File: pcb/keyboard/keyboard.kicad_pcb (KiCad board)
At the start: 2 copper layers, 137.2 x 109.2 mm, 96 parts, among them J1 Audio-Jack-4, J2 sidebutton, SW1 RESET_SW, U1 Arduino_Pro_Micro, U2 Arduino_Pro_Micro

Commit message: add LED
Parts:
- added D53: LED, LEDs:LED_D3.0mm, F.Cu at (116.2, 39.4)
- added D54: LED, LEDs:LED_D3.0mm, F.Cu at (116.2, 43.8)
- added D55: LED, LEDs:LED_D3.0mm, F.Cu at (116.2, 48.3)
- added R3: 100Ω, Resistors_THT:R_Axial_DIN0204_L3.6mm_D1.6mm_P7.62mm_Horizontal, F.Cu at (119.4, 28.6)
- added R5: 100Ω, Resistors_THT:R_Axial_DIN0204_L3.6mm_D1.6mm_P7.62mm_Horizontal, F.Cu at (117.5, 28.6)
- added R6: 100Ω, Resistors_THT:R_Axial_DIN0204_L3.6mm_D1.6mm_P7.62mm_Horizontal, F.Cu at (115.6, 28.6)
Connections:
- U1 pad 18: Net-(U1-Pad18) -> /LED3
- U1 pad 19: Net-(U1-Pad19) -> /LED2
- U1 pad 20: Net-(U1-Pad20) -> /LED1
- U2 pad 18: Net-(U2-Pad18) -> /LED3
- U2 pad 19: Net-(U2-Pad19) -> /LED2
- U2 pad 20: Net-(U2-Pad20) -> /LED1
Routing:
- net /LED3: track 0.00 -> 56.0 mm, vias 0 -> 11
- net /LED2: track 0.00 -> 54.1 mm, vias 0 -> 14
- net /LED1: track 0.00 -> 52.8 mm, vias 0 -> 16
- net +5V: track 82.9 -> 101.7 mm, vias 1 -> 2
- net Net-(D55-Pad2): track 0.00 -> 14.1 mm
- net Net-(D54-Pad2): track 0.00 -> 8.15 mm
- net Net-(D53-Pad2): track 0.00 -> 3.44 mm
- net /SDA: track 65.7 -> 68.0 mm
- net /ROW4: track 300.2 -> 301.8 mm
- net /COL0: track 110.5 -> 112.1 mm
- net /SCL: track 60.0 -> 61.4 mm
- net /COL4: track 153.4 -> 153.9 mm

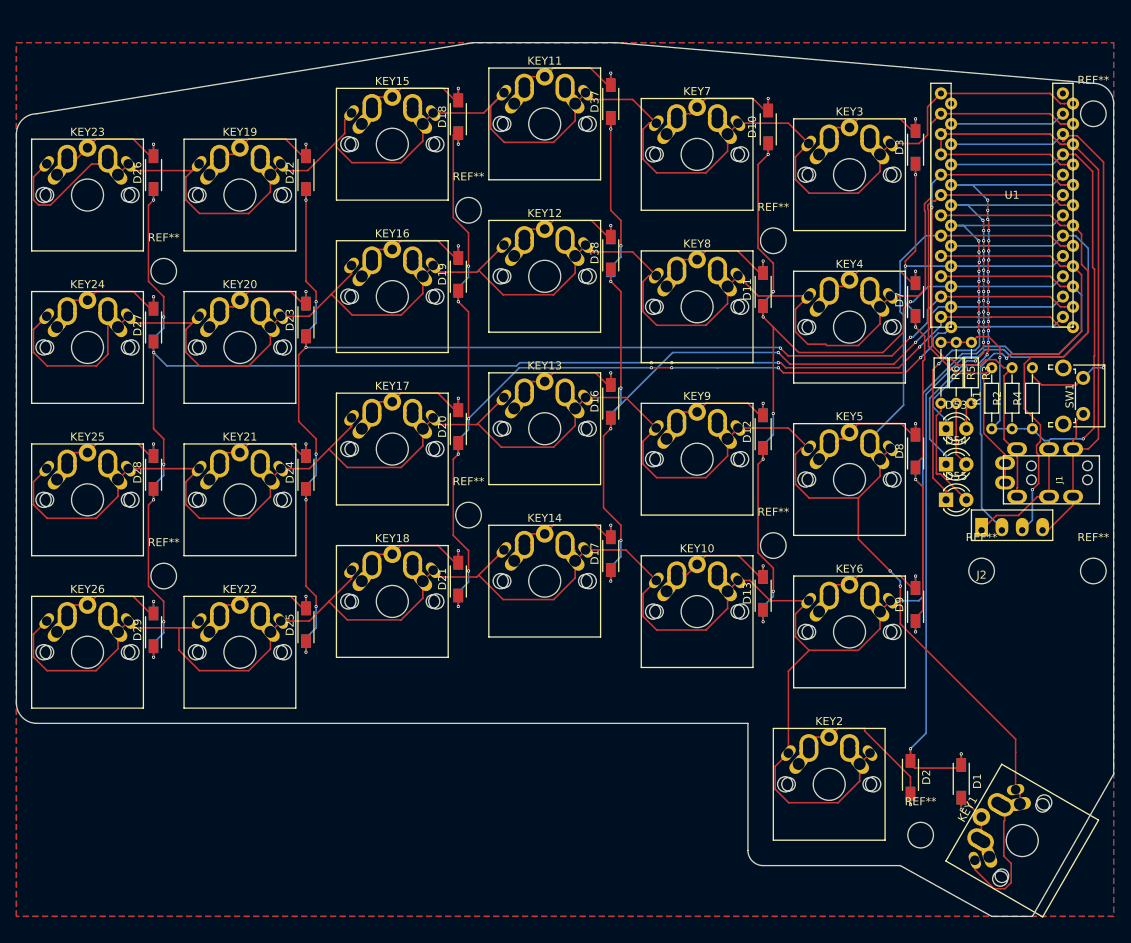
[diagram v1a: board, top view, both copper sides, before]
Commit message: emlarge via drill size 0.2032 -> 0.3
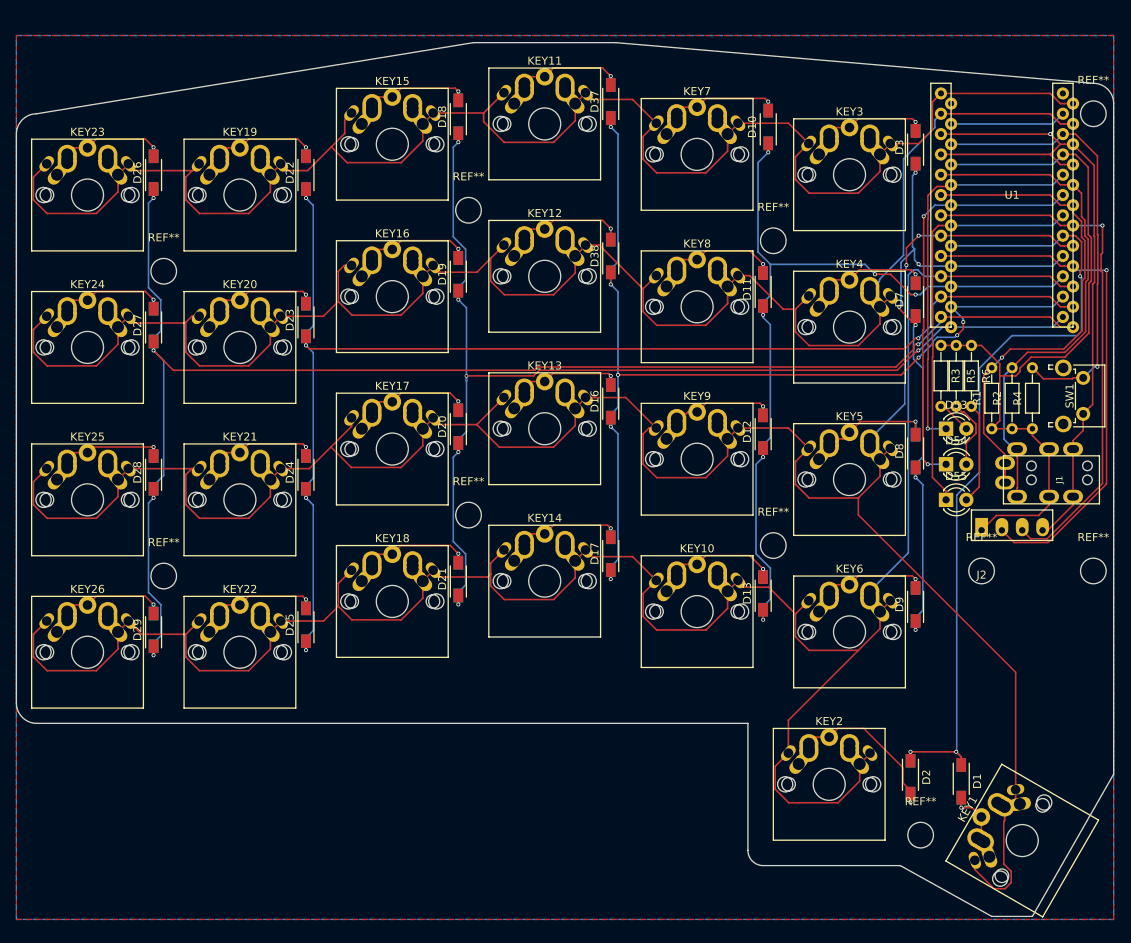
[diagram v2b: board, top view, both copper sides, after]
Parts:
- moved R3 3.83 mm to (115.6, 29.0)
- moved R6 3.83 mm to (119.4, 29.0)
- moved D38 0.38 mm to (74.3, 17.8)
- moved R5 0.38 mm to (117.5, 29.0)
- moved D15 0.26 mm to (74.3, 17.8)
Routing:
- net /ROW4: track 301.8 -> 287.8 mm
- net GND: track 111.8 -> 104.2 mm, vias 0 -> 1
- net /COL4: track 153.9 -> 147.0 mm, vias 11 -> 6
- net +5V: track 101.7 -> 95.3 mm, vias 2 -> 0
- net /COL0: track 112.1 -> 105.8 mm, vias 2 -> 3
- net /COL2: track 115.1 -> 109.0 mm, vias 8 -> 6
- net /ROW1: track 234.2 -> 228.5 mm
- net /COL3: track 136.0 -> 130.4 mm, vias 9 -> 8
- net /LED3: track 56.0 -> 51.4 mm, vias 11 -> 0
- net /LED1: track 52.8 -> 49.4 mm, vias 16 -> 1
- net /RST: track 59.0 -> 55.7 mm
- net /SDA: track 68.0 -> 64.8 mm, vias 1 -> 0
- net /COL5: track 170.1 -> 167.1 mm, vias 9 -> 5
- net /Y: track 63.6 -> 66.4 mm
- net /X: track 62.1 -> 64.9 mm
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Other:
- net class Default: via_dia 0.4 -> 0.5; via_drill 0.2032 -> 0.3
- rule via_min_drill: 0.2032 -> 0.3

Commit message: improve silk and holes
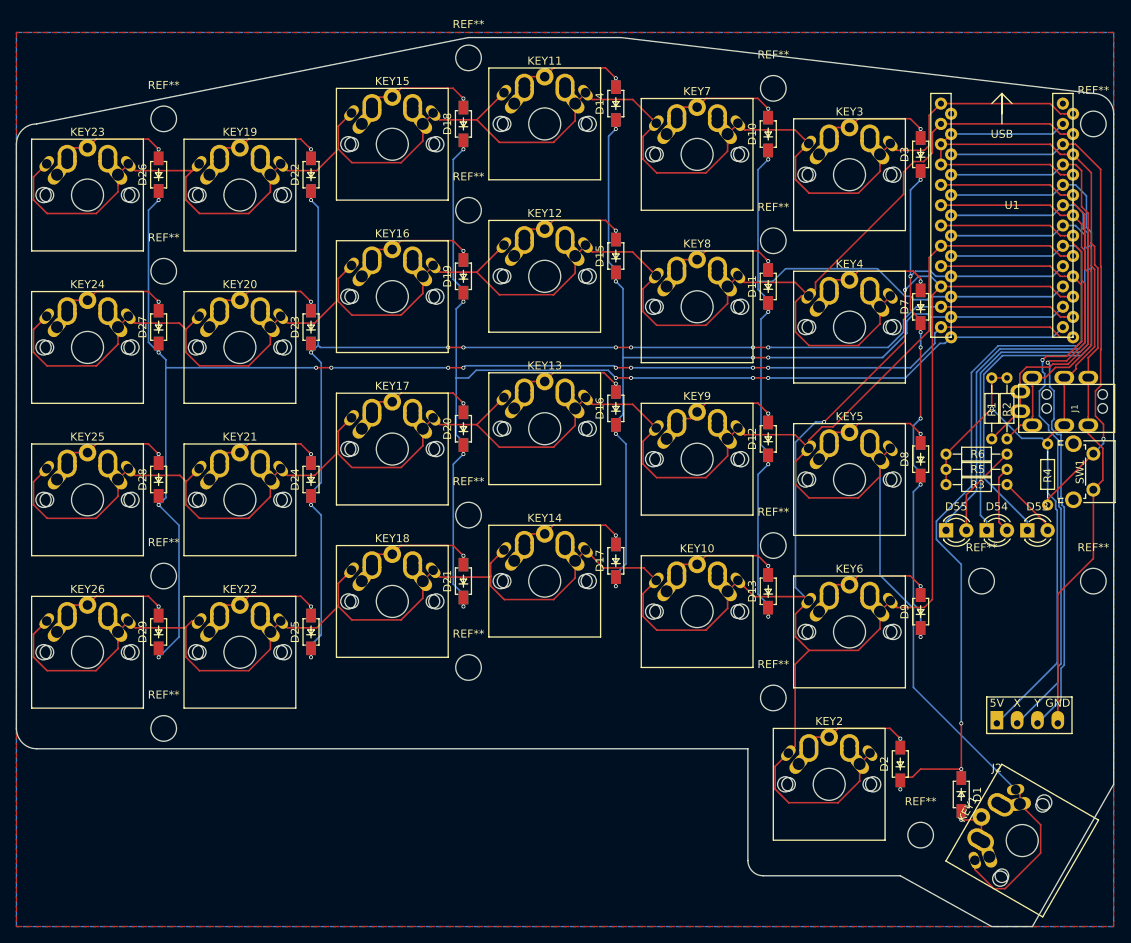
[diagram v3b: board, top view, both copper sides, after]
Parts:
- added REF**: MountingHole_3.2mm_M3, Mounting_Holes:MountingHole_3.2mm_M3, F.Cu at (18.4, 76.8)
- added REF**: MountingHole_3.2mm_M3, Mounting_Holes:MountingHole_3.2mm_M3, F.Cu at (18.4, 0.64)
- added REF**: MountingHole_3.2mm_M3, Mounting_Holes:MountingHole_3.2mm_M3, F.Cu at (94.6, -3.17)
- added REF**: MountingHole_3.2mm_M3, Mounting_Holes:MountingHole_3.2mm_M3, F.Cu at (94.6, 73.0)
- added REF**: MountingHole_3.2mm_M3, Mounting_Holes:MountingHole_3.2mm_M3, F.Cu at (56.5, -6.99)
- added REF**: MountingHole_3.2mm_M3, Mounting_Holes:MountingHole_3.2mm_M3, F.Cu at (56.5, 69.2)
- D14, D15: moved to F.Cu
- D37, D38: moved to B.Cu
- D53, D54, D55: footprint LEDs:LED_D3.0mm -> 4x6t2:LED_D3.0mm
- R1, R2, R3, R4, R5, R6: footprint Resistors_THT:R_Axial_DIN0204_L3.6mm_D1.6mm_P7.62mm_Horizontal -> 4x6t2:R_Axial
- SW1: footprint Buttons_Switches_THT:SW_Tactile_SPST_Angled_PTS645Vx31-2LFS -> 4x6t2:SW_Tactile_SPST_Angled
- moved J2 24.2 mm to (122.6, 76.2)
- moved R3 17.4 mm to (116.2, 46.4), turned to 0 degrees
- moved D53 16.3 mm to (126.4, 52.1)
- moved R5 15.5 mm to (116.2, 44.5), turned to 0 degrees
- moved R6 14.0 mm to (116.2, 42.5), turned to 0 degrees
- moved D54 9.69 mm to (121.3, 52.1)
- moved SW1 9.55 mm to (134.6, 42.5)
- moved J1 9.13 mm to (137.3, 36.8)
- moved R2 6.38 mm to (123.8, 33.0), turned to 270 degrees
- moved R1 6.35 mm to (121.9, 33.0), turned to 270 degrees
- moved D55 3.81 mm to (116.2, 52.1)
- moved R4 2.69 mm to (128.9, 41.3), turned to 270 degrees
- moved D2 2.08 mm to (110.5, 81.3), turned to 90 degrees
- moved D5 2.08 mm to (110.5, 81.3), turned to 90 degrees
- moved D1 1.65 mm to (118.1, 85.1)
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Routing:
- net /ROW4: track 287.8 -> 338.0 mm, vias 0 -> 2
- net +5V: track 95.3 -> 120.6 mm, vias 0 -> 1
- net GND: track 104.2 -> 128.9 mm, vias 1 -> 0
- net /LED1: track 49.4 -> 73.7 mm, vias 1 -> 0
- net /Y: track 66.4 -> 84.5 mm
- net /LED2: track 52.1 -> 69.0 mm, vias 2 -> 0
- net /LED3: track 51.4 -> 67.6 mm
- net /X: track 64.9 -> 80.7 mm
- net /RST: track 55.7 -> 66.1 mm
- net /SDA: track 64.8 -> 55.7 mm
- net /SCL: track 62.6 -> 53.7 mm, vias 1 -> 0
- net /ROW2: track 302.0 -> 308.1 mm, vias 2 -> 0
- net Net-(D2-Pad2): track 22.9 -> 17.8 mm
- net /ROW1: track 228.5 -> 233.3 mm
- net /COL0: track 105.8 -> 110.5 mm
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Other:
- board size 137.2 x 109.2 mm -> 137.2 x 111.1 mm

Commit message: fix schematic
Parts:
- turned D1 to 90 degrees
- turned D4 to 90 degrees
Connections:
- D1 pad 1: /COL0 -> Net-(D1-Pad1)
- D1 pad 2: Net-(D1-Pad2) -> /COL0
- D10 pad 1: /COL2 -> Net-(D10-Pad1)
- D10 pad 2: Net-(D10-Pad2) -> /COL2
- D11 pad 1: /COL2 -> Net-(D11-Pad1)
- D11 pad 2: Net-(D11-Pad2) -> /COL2
- D12 pad 1: /COL2 -> Net-(D12-Pad1)
- D12 pad 2: Net-(D12-Pad2) -> /COL2
- D13 pad 1: /COL2 -> Net-(D13-Pad1)
- D13 pad 2: Net-(D13-Pad2) -> /COL2
- D14 pad 1: /COL3 -> Net-(D14-Pad1)
- D14 pad 2: Net-(D14-Pad2) -> /COL3
- D15 pad 1: /COL3 -> Net-(D15-Pad1)
- D15 pad 2: Net-(D15-Pad2) -> /COL3
- D16 pad 1: /COL3 -> Net-(D16-Pad1)
- D16 pad 2: Net-(D16-Pad2) -> /COL3
- D17 pad 1: /COL3 -> Net-(D17-Pad1)
- D17 pad 2: Net-(D17-Pad2) -> /COL3
- D18 pad 1: /COL4 -> Net-(D18-Pad1)
- D18 pad 2: Net-(D18-Pad2) -> /COL4
- D19 pad 1: /COL4 -> Net-(D19-Pad1)
- D19 pad 2: Net-(D19-Pad2) -> /COL4
- D2 pad 1: /COL0 -> Net-(D2-Pad1)
- D2 pad 2: Net-(D2-Pad2) -> /COL0
- D20 pad 1: /COL4 -> Net-(D20-Pad1)
- D20 pad 2: Net-(D20-Pad2) -> /COL4
- D21 pad 1: /COL4 -> Net-(D21-Pad1)
- D21 pad 2: Net-(D21-Pad2) -> /COL4
- D22 pad 1: /COL5 -> Net-(D22-Pad1)
- D22 pad 2: Net-(D22-Pad2) -> /COL5
- D23 pad 1: /COL5 -> Net-(D23-Pad1)
- D23 pad 2: Net-(D23-Pad2) -> /COL5
- D24 pad 1: /COL5 -> Net-(D24-Pad1)
- D24 pad 2: Net-(D24-Pad2) -> /COL5
- D25 pad 1: /COL5 -> Net-(D25-Pad1)
- D25 pad 2: Net-(D25-Pad2) -> /COL5
- D26 pad 1: /COL6 -> Net-(D26-Pad1)
- D26 pad 2: Net-(D26-Pad2) -> /COL6
- D27 pad 1: /COL6 -> Net-(D27-Pad1)
- D27 pad 2: Net-(D27-Pad2) -> /COL6
- D28 pad 1: /COL6 -> Net-(D28-Pad1)
- D28 pad 2: Net-(D28-Pad2) -> /COL6
- D29 pad 1: /COL6 -> Net-(D29-Pad1)
- D29 pad 2: Net-(D29-Pad2) -> /COL6
- D3 pad 1: /COL1 -> Net-(D3-Pad1)
- D3 pad 2: Net-(D3-Pad2) -> /COL1
- D30 pad 1: /COL1 -> Net-(D30-Pad1)
- D30 pad 2: Net-(D30-Pad2) -> /COL1
- D31 pad 1: /COL1 -> Net-(D31-Pad1)
- D31 pad 2: Net-(D31-Pad2) -> /COL1
- D32 pad 1: /COL1 -> Net-(D32-Pad1)
- D32 pad 2: Net-(D32-Pad2) -> /COL1
- D33 pad 1: /COL2 -> Net-(D10-Pad1)
- D33 pad 2: Net-(D10-Pad2) -> /COL2
- D34 pad 1: /COL2 -> Net-(D11-Pad1)
- D34 pad 2: Net-(D11-Pad2) -> /COL2
- D35 pad 1: /COL2 -> Net-(D12-Pad1)
- D35 pad 2: Net-(D12-Pad2) -> /COL2
- D36 pad 1: /COL2 -> Net-(D13-Pad1)
- D36 pad 2: Net-(D13-Pad2) -> /COL2
- D37 pad 1: /COL3 -> Net-(D14-Pad1)
- D37 pad 2: Net-(D14-Pad2) -> /COL3
- D38 pad 1: /COL3 -> Net-(D15-Pad1)
- D38 pad 2: Net-(D15-Pad2) -> /COL3
- D39 pad 1: /COL3 -> Net-(D16-Pad1)
- D39 pad 2: Net-(D16-Pad2) -> /COL3
- D4 pad 1: /COL0 -> Net-(D1-Pad1)
- D4 pad 2: Net-(D1-Pad2) -> /COL0
- D40 pad 1: /COL3 -> Net-(D17-Pad1)
- D40 pad 2: Net-(D17-Pad2) -> /COL3
- D41 pad 1: /COL4 -> Net-(D18-Pad1)
- D41 pad 2: Net-(D18-Pad2) -> /COL4
- D42 pad 1: /COL4 -> Net-(D19-Pad1)
- D42 pad 2: Net-(D19-Pad2) -> /COL4
- D43 pad 1: /COL4 -> Net-(D20-Pad1)
- D43 pad 2: Net-(D20-Pad2) -> /COL4
- D44 pad 1: /COL4 -> Net-(D21-Pad1)
- D44 pad 2: Net-(D21-Pad2) -> /COL4
- D45 pad 1: /COL5 -> Net-(D22-Pad1)
- D45 pad 2: Net-(D22-Pad2) -> /COL5
- D46 pad 1: /COL5 -> Net-(D23-Pad1)
- D46 pad 2: Net-(D23-Pad2) -> /COL5
- D47 pad 1: /COL5 -> Net-(D24-Pad1)
- D47 pad 2: Net-(D24-Pad2) -> /COL5
- D48 pad 1: /COL5 -> Net-(D25-Pad1)
- D48 pad 2: Net-(D25-Pad2) -> /COL5
- D49 pad 1: /COL6 -> Net-(D26-Pad1)
- D49 pad 2: Net-(D26-Pad2) -> /COL6
- D5 pad 1: /COL0 -> Net-(D2-Pad1)
- D5 pad 2: Net-(D2-Pad2) -> /COL0
- D50 pad 1: /COL6 -> Net-(D27-Pad1)
- D50 pad 2: Net-(D27-Pad2) -> /COL6
- D51 pad 1: /COL6 -> Net-(D28-Pad1)
- D51 pad 2: Net-(D28-Pad2) -> /COL6
- D52 pad 1: /COL6 -> Net-(D29-Pad1)
- D52 pad 2: Net-(D29-Pad2) -> /COL6
- D6 pad 1: /COL1 -> Net-(D3-Pad1)
- D6 pad 2: Net-(D3-Pad2) -> /COL1
- D7 pad 1: /COL1 -> Net-(D30-Pad1)
- D7 pad 2: Net-(D30-Pad2) -> /COL1
- D8 pad 1: /COL1 -> Net-(D31-Pad1)
- D8 pad 2: Net-(D31-Pad2) -> /COL1
- D9 pad 1: /COL1 -> Net-(D32-Pad1)
- D9 pad 2: Net-(D32-Pad2) -> /COL1
- KEY1 pad 2: Net-(D1-Pad2) -> Net-(D1-Pad1)
- KEY10 pad 2: Net-(D13-Pad2) -> Net-(D13-Pad1)
- KEY11 pad 2: Net-(D14-Pad2) -> Net-(D14-Pad1)
- KEY12 pad 2: Net-(D15-Pad2) -> Net-(D15-Pad1)
- KEY13 pad 2: Net-(D16-Pad2) -> Net-(D16-Pad1)
- KEY14 pad 2: Net-(D17-Pad2) -> Net-(D17-Pad1)
- KEY15 pad 2: Net-(D18-Pad2) -> Net-(D18-Pad1)
- KEY16 pad 2: Net-(D19-Pad2) -> Net-(D19-Pad1)
- KEY17 pad 2: Net-(D20-Pad2) -> Net-(D20-Pad1)
- KEY18 pad 2: Net-(D21-Pad2) -> Net-(D21-Pad1)
- KEY19 pad 2: Net-(D22-Pad2) -> Net-(D22-Pad1)
- KEY2 pad 2: Net-(D2-Pad2) -> Net-(D2-Pad1)
- KEY20 pad 2: Net-(D23-Pad2) -> Net-(D23-Pad1)
- KEY21 pad 2: Net-(D24-Pad2) -> Net-(D24-Pad1)
- KEY22 pad 2: Net-(D25-Pad2) -> Net-(D25-Pad1)
- KEY23 pad 2: Net-(D26-Pad2) -> Net-(D26-Pad1)
- KEY24 pad 2: Net-(D27-Pad2) -> Net-(D27-Pad1)
- KEY25 pad 2: Net-(D28-Pad2) -> Net-(D28-Pad1)
- KEY26 pad 2: Net-(D29-Pad2) -> Net-(D29-Pad1)
- KEY3 pad 2: Net-(D3-Pad2) -> Net-(D3-Pad1)
- KEY4 pad 2: Net-(D30-Pad2) -> Net-(D30-Pad1)
- KEY5 pad 2: Net-(D31-Pad2) -> Net-(D31-Pad1)
- KEY6 pad 2: Net-(D32-Pad2) -> Net-(D32-Pad1)
- KEY7 pad 2: Net-(D10-Pad2) -> Net-(D10-Pad1)
- KEY8 pad 2: Net-(D11-Pad2) -> Net-(D11-Pad1)
- KEY9 pad 2: Net-(D12-Pad2) -> Net-(D12-Pad1)
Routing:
- net /ROW4: track 338.0 -> 0.00 mm, vias 2 -> 0
- net /ROW2: track 308.1 -> 0.00 mm
- net /ROW1: track 233.3 -> 0.00 mm
- net /ROW0: track 216.1 -> 0.00 mm
- net /COL6: track 190.2 -> 0.00 mm, vias 12 -> 0
- net /COL5: track 167.1 -> 0.00 mm, vias 10 -> 0
- net /COL4: track 146.9 -> 0.00 mm, vias 8 -> 0
- net GND: track 128.9 -> 0.00 mm
- net /COL3: track 126.1 -> 0.00 mm, vias 6 -> 0
- net +5V: track 120.6 -> 0.00 mm, vias 1 -> 0
- net /COL0: track 110.5 -> 0.00 mm, vias 3 -> 0
- net /COL2: track 108.7 -> 0.00 mm, vias 4 -> 0
- net /COL1: track 87.4 -> 0.00 mm, vias 7 -> 0
- net /Y: track 84.5 -> 0.00 mm, vias 1 -> 0
- net /X: track 80.7 -> 0.00 mm, vias 1 -> 0
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- removed copper zone on B.Cu, net GND
- removed copper zone on F.Cu, net GND
